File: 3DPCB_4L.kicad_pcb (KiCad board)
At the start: 4 copper layers, 100 x 60 mm, 802 parts, among them IC1 A5984_LP, IC2 A5984_LP, IC3 A5984_LP, IC4 A5984_LP, IC5 A5984_LP, IC6 MP9943, J10 , J11 , J12 , J13 , J14 , J15 , J16 , J2 , J3 , J4 , J5 , J6 , J7 , J8 , J9 , K1 CONN_3, K2 CONN_3, K3 CONN_3, K4 CONN_3, K5 CONN_3, K6 CONN_3, K7 CONN_3, K8 CONN_3, K9 CONN_3, P1 CONN_8, P11 CONN_3X2, P12 CONN_3X2, P13 CONN_4, P2 CONN_8, P3 CONN_01X02, P5 CONN_4, P6 CONN_4, P7 CONN_4, P8 CONN_02X03, P9 CONN_4, U1 CONN_4_LERCHE, U10 MICRO-SD, U11 TC4427, U12 MCP4728, U13 CONN_4_LERCHE, U15 SPST_MOMENTARY, U16 CONN_4_LERCHE, U2 SPST_MOMENTARY, U21 CONN_4_LERCHE, U22 CONN_4_LERCHE, U23 MCP4728, U24 IRFH5302, U25 CONN_4_LERCHE, U3 BSS84, U4 CONN_4_LERCHE, U5 IRFH5302, U6 LPC1768_TQFP100, U7 IRFH5302, U8 IRFH5302, U9 TC4427

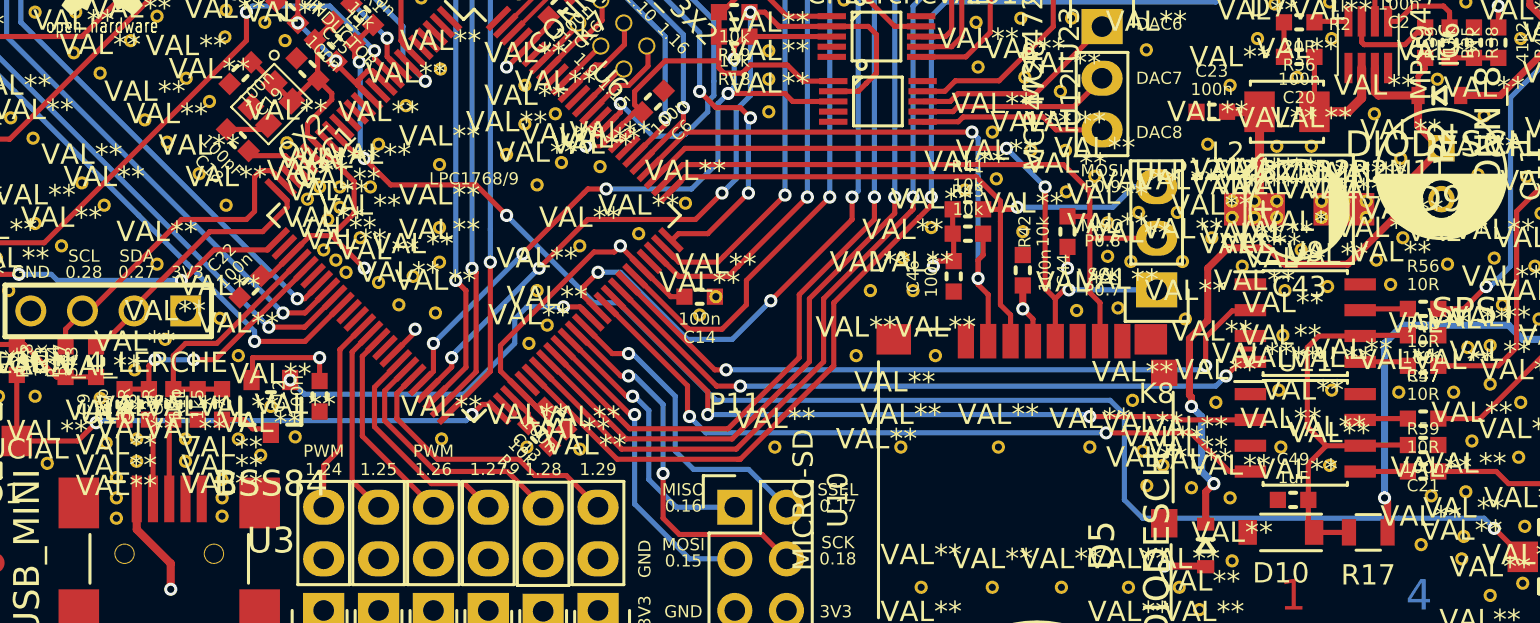
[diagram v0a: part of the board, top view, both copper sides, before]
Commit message: Smaller traces, length matching USB
Smaller traces, length matching USB
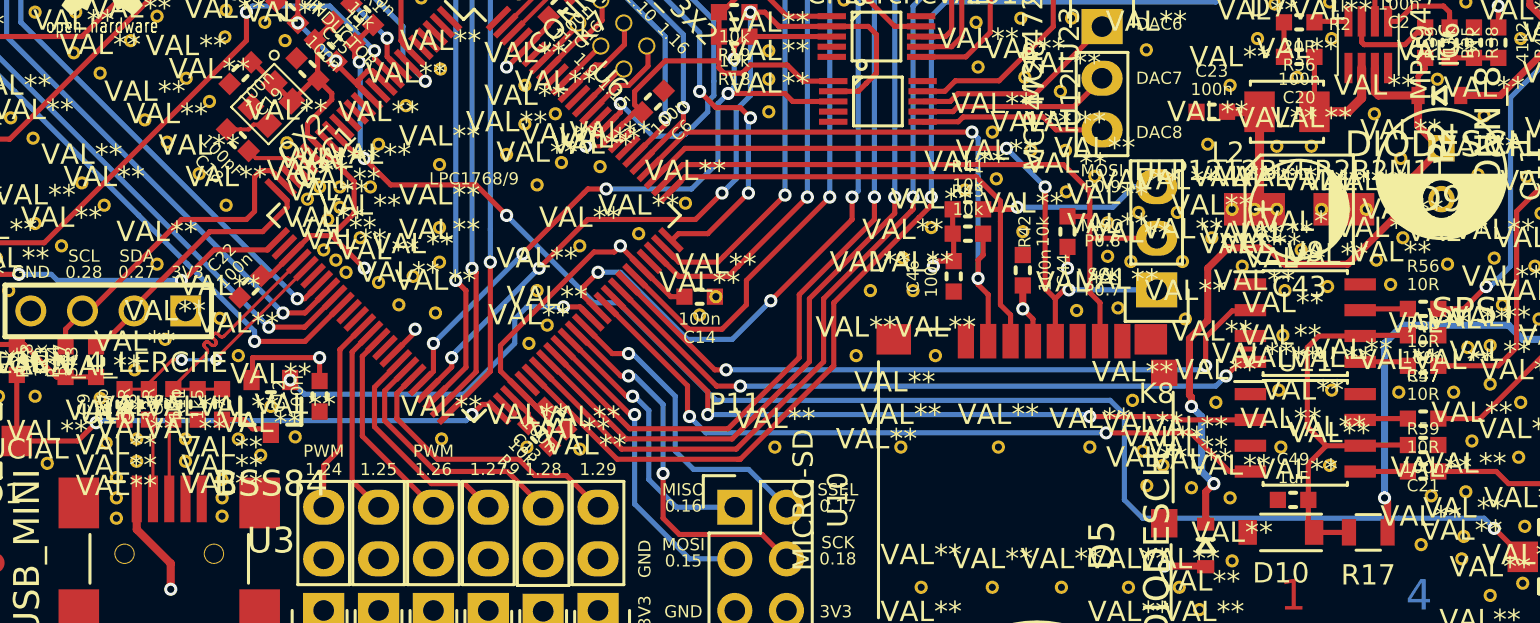
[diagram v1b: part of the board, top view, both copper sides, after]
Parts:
- removed the ? at (199.8, 172.8)
- removed the ? at (204.2, 172.8)
- removed the ? at (205.3, 172.8)
- removed the ? at (206.4, 172.8)
- removed the ? at (199.8, 173.6)
- removed the ? at (200.9, 172.8)
- moved ? 1.17 mm to (199.8, 173.2)
- moved ? 1.17 mm to (200.9, 173.2)
- moved ? 0.40 mm to (205.3, 173.2)
- moved ? 0.40 mm to (206.4, 173.2)
- moved ? 0.40 mm to (204.2, 173.2)
- moved ? 0.40 mm to (202.0, 173.2)
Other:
- net class Default: via_dia 0.65 -> 0.6; via_drill 0.35 -> 0.3
- rule via_min_drill: 0.35 -> 0.3
- rule via_min_size: 0.65 -> 0.6

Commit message: Rewiring some things.
Rewiring some things.
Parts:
- moved ? 0.46 mm to (149.7, 178.2)
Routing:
- net USB_D+: track 12.5 -> 16.3 mm
- net USB_D-: track 11.6 -> 12.3 mm

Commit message: Minor adjustments.
Getting ready to order boards now.
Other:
- outline, holes or cut-outs redrawn
- board text added: "3DPCB - Three Dimensional Printer Controller Board Smoothie-compatible - www.smoothieware.org"
- board text added: "3DPCB www.LercheTech.dk C. Lerche - 2017"
- board text removed: "3DPCB www.LercheTech.dk C. Lerche - 2016"
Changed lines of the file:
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@@
     (links 1102)
     (no_connects 0)
-    (area 126.046317 131.0284 237.651491 200.475)
+    (area 129.949999 135.449999 230.050001 195.550001)
     (thickness 1.6)
-    (drawings 163)
+    (drawings 168)
     (tracks 1762)
     (zones 0)
@@
     (visible_elements 7FFC7FFF)
     (pcbplotparams
-      (layerselection 0x00030_80000001)
+      (layerselection 0x010f0_80000007)
       (usegerberextensions true)
       (excludeedgelayer true)
@@
     )
   )
+  (gr_line (start 130 192.5) (end 130 138.5) (layer Edge.Cuts) (width 0.1))
+  (gr_line (start 227 195.5) (end 133 195.5) (layer Edge.Cuts) (width 0.1))
+  (gr_line (start 230 138.5) (end 230 192.5) (layer Edge.Cuts) (width 0.1))
+  (gr_line (start 133 135.5) (end 227 135.5) (layer Edge.Cuts) (width 0.1))
+  (gr_arc (start 133 192.5) (end 133 195.5) (angle 90) (layer Edge.Cuts) (width 0.1))
+  (gr_arc (start 227 192.5) (end 230 192.5) (angle 90) (layer Edge.Cuts) (width 0.1))
+  (gr_arc (start 227 138.5) (end 227 135.5) (angle 90) (layer Edge.Cuts) (width 0.1))
+  (gr_arc (start 133 138.5) (end 130 138.5) (angle 90) (layer Edge.Cuts) (width 0.1))
+  (gr_text "3DPCB - Three Dimensional Printer Controller Board\nSmoothie-compatible - www.smoothieware.org" (at 180 151.2) (layer B.SilkS)
+    (effects (font (size 1.5 1.5) (thickness 0.3)) (justify mirror))
+  )
   (gr_text AGND (at 139.2 154.6 45) (layer F.SilkS)
     (effects (font (size 0.6 0.6) (thickness 0.1)))
@@
     (effects (font (size 0.6 0.6) (thickness 0.1)))
   )
-  (gr_text "3DPCB\nwww.LercheTech.dk\nC. Lerche - 2016" (at 184.5 161) (layer F.SilkS)
+  (gr_text "3DPCB\nwww.LercheTech.dk\nC. Lerche - 2017" (at 184.5 161) (layer F.SilkS)
     (effects (font (size 1 1) (thickness 0.2)))
   )
@@
     (effects (font (size 0.6 0.6) (thickness 0.1)))
   )
-  (gr_line (start 130 135.5) (end 130 195.5) (angle 90) (layer Edge.Cuts) (width 0.15))
-  (gr_line (start 230 135.5) (end 130 135.5) (angle 90) (layer Edge.Cuts) (width 0.15))
-  (gr_line (start 230 195.5) (end 230 135.5) (angle 90) (layer Edge.Cuts) (width 0.15))
-  (gr_line (start 130 195.5) (end 230 195.5) (angle 90) (layer Edge.Cuts) (width 0.15))
   (segment (start 200.125 180.075) (end 200.8 180.075) (width 0.254) (layer F.Cu) (net 0))
   (segment (start 211.1 153.1) (end 210.4507 153.1) (width 0.254) (layer F.Cu) (net 1))

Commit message: Updated pinheader
Updated pinheader
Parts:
- ? (x571): value VAL** -> (none)
- K1, K2, K3, K4, K5, K6, K8, K9: footprint Pin_Headers:Pin_Header_Straight_1x03 -> LercheTech:Lerche_3P_2.54mm
- P3: footprint Pin_Headers:Pin_Header_Straight_1x02_Pitch2.54mm -> LercheTech:Lerche_2P_2.54mm
- moved K5 2.58 mm to (165.9, 190.4), turned to 90 degrees
- moved K8 2.57 mm to (196.1, 174.6), turned to 90 degrees
- moved K9 2.54 mm to (193.4, 166.8), turned to 270 degrees
- moved K1 2.54 mm to (155.1, 190.4), turned to 90 degrees
- moved K2 2.54 mm to (157.8, 190.4), turned to 90 degrees
- moved K3 2.54 mm to (160.5, 190.4), turned to 90 degrees
- moved K4 2.54 mm to (163.2, 190.4), turned to 90 degrees
- moved K6 2.54 mm to (168.6, 190.4), turned to 90 degrees
- moved P3 1.24 mm to (141.6, 156.1), turned to 90 degrees
